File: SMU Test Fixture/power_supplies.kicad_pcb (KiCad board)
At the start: 2 copper layers, 84.9 x 130.1 mm, 47 parts, among them J13 Hot_Spade, J14 Power Outputs, J15 Neutral_Spade, Q1 IRFL014, Q2 IRFL014, T1 VPP28-1060, U10 LT3045, U11 LT1086-12, U12 LT3094, U9 LT1086-5.0

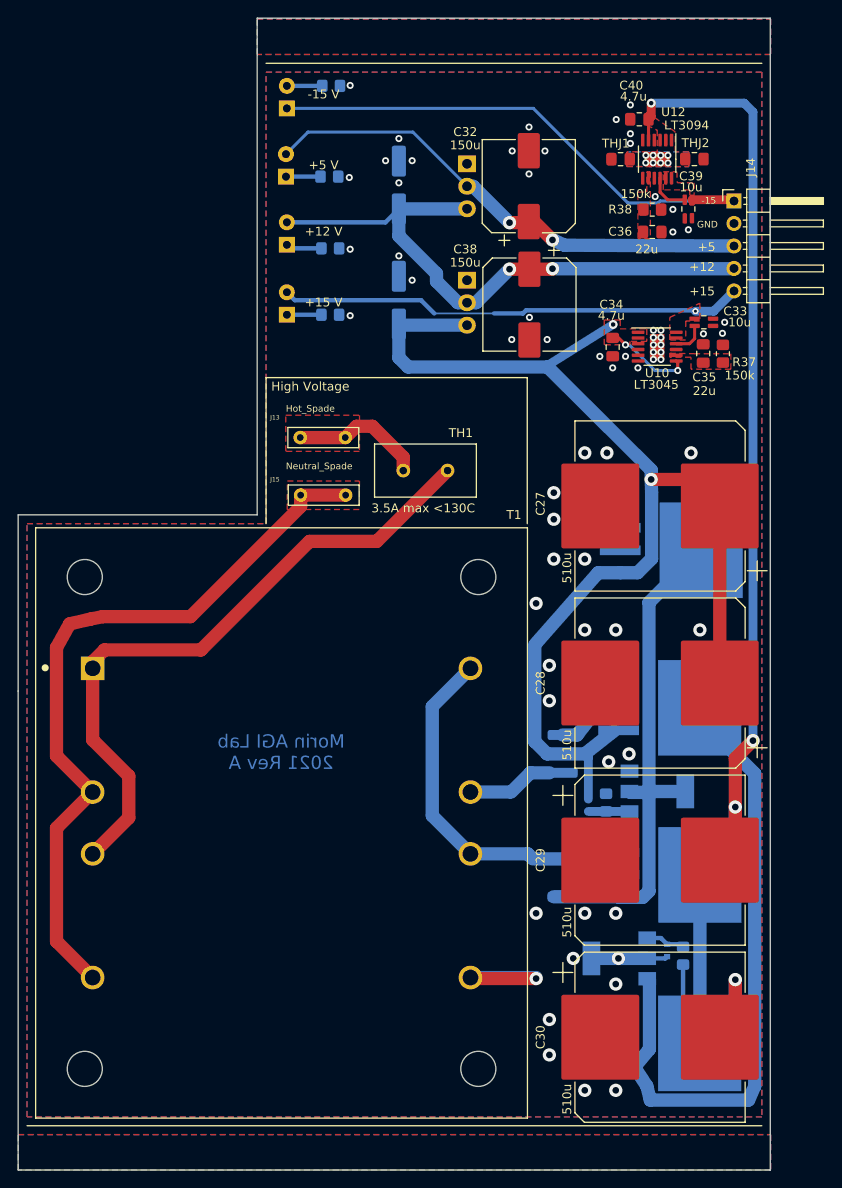
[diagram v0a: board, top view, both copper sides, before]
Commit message: Improved crowbar performance. Posted for reddit design review.
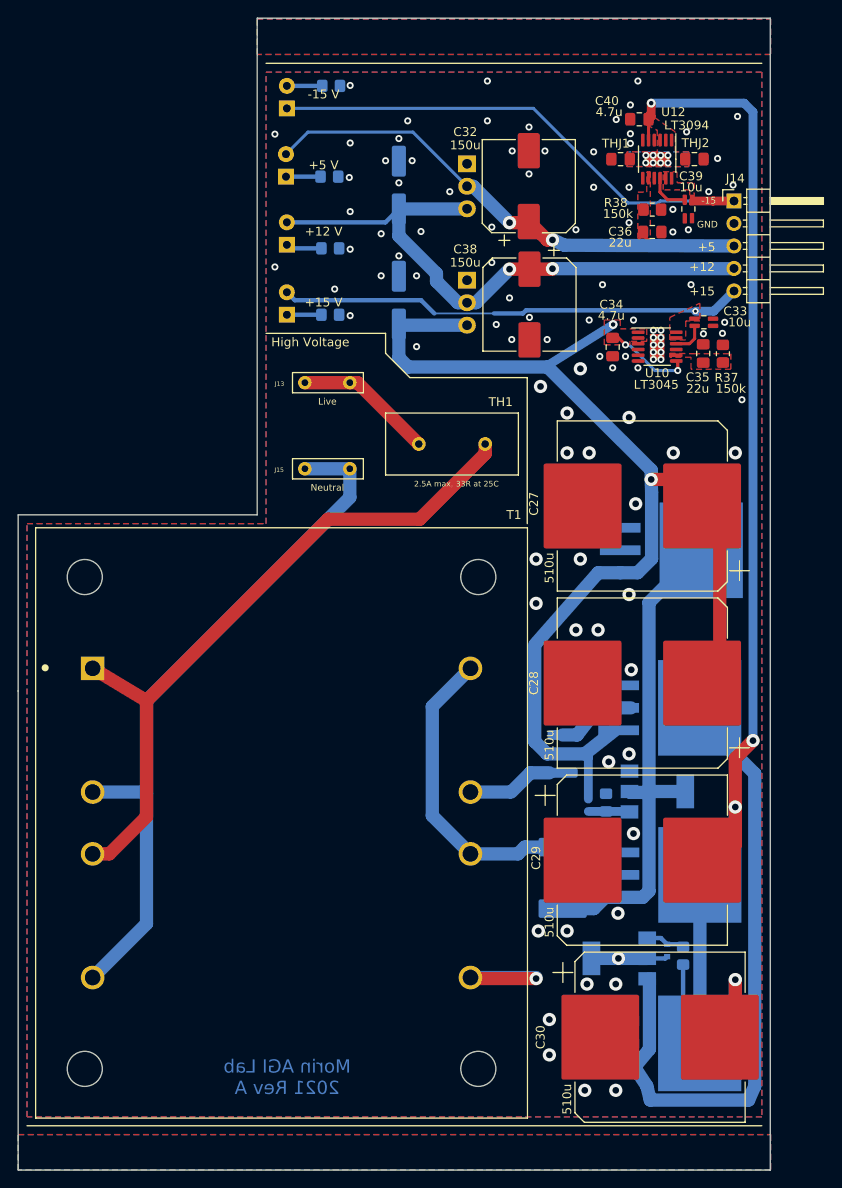
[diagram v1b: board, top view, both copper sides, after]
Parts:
- D39, D46: value 20V -> 16V
- F1: footprint Fuse:Fuse_1812_4532Metric -> Fuse:Fuse_2920_7451Metric_Pad2.10x5.45mm_HandSolder
- F2: value 1 A -> 500mA
- J13: value Hot_Spade -> Live
- J15: value Neutral_Spade -> Neutral
- R39, R40: value 1K -> 180R
- TH1: value 3.5A max <130C -> 2.5A max, 33R at 25C; footprint MAGI_Footprints:NTC d=11.5 p=5mm w=6mm -> MAGI_Footprints:NTC d=15 p=7p5mm w=7mm
- moved J13 6.22 mm to (138.9, 70.2)
- moved TH1 4.24 mm to (153.0, 77.0)
- moved J15 3.01 mm to (138.9, 79.9)
- moved C27 2.00 mm to (174.5, 84.0)
- moved C28 2.00 mm to (174.5, 104.0)
- moved C29 2.00 mm to (174.5, 124.0)
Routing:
- net Net-(T1-Pad1): track 74.1 -> 78.9 mm
- net Net-(J15-Pad1): track 83.1 -> 80.7 mm
- net Net-(J13-Pad1): track 15.1 -> 15.7 mm
- net Net-(F1-Pad2): track 35.8 -> 35.3 mm
- net GND: vias 68 -> 104
- removed copper zone on F.Cu, net Net-(J13-Pad1)
- removed copper zone on F.Cu, net Net-(J15-Pad1)
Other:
- net class HV: clearance 2 -> 4; trace_width 1.5 -> 1; via_dia 1.5 -> 1

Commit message: Route LTC2966 addition and remove pin 2 connections.
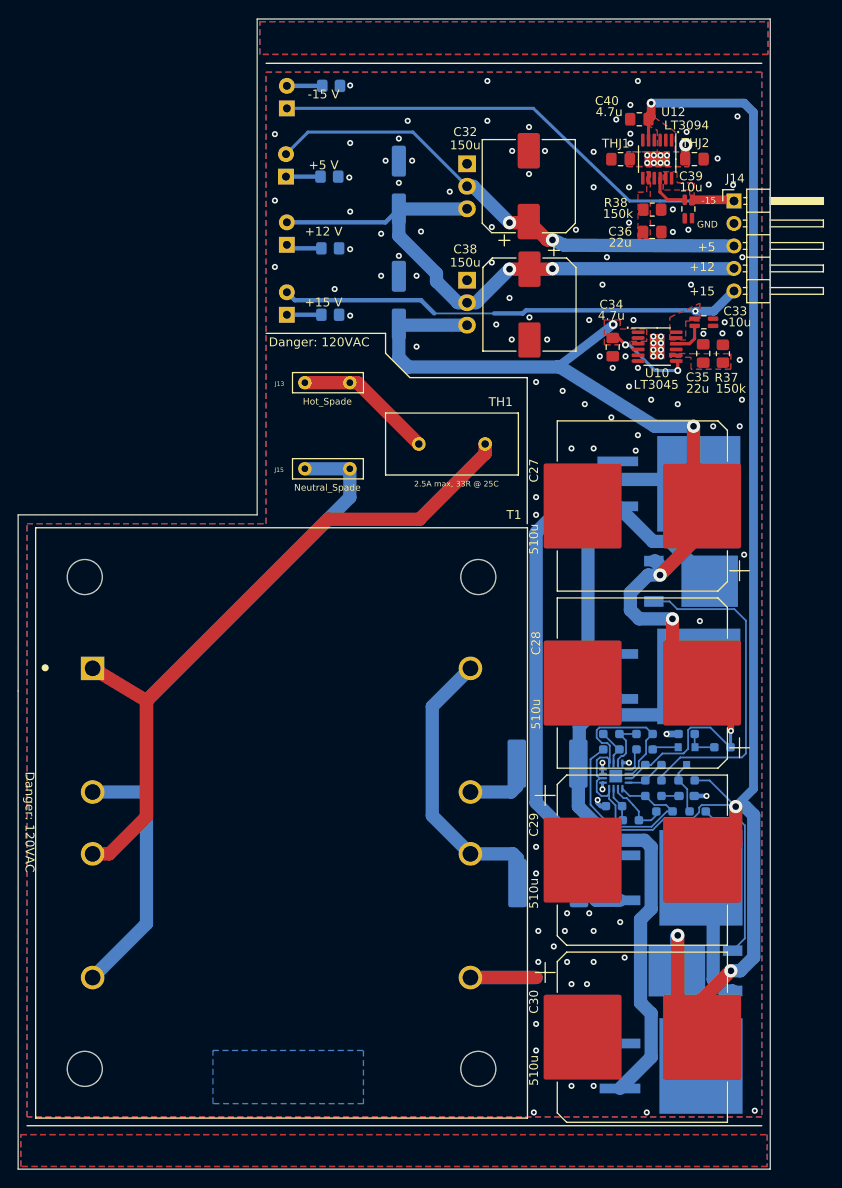
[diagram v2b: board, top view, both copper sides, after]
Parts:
- removed D39, D46: 16V, Diode_SMD:D_SOD-523
- added C41: 1u, Capacitor_SMD:C_0603_1608Metric_Pad1.08x0.95mm_HandSolder, B.Cu at (179.5, 116.8)
- added Q3: MMBT3906, Package_TO_SOT_SMD:SOT-23, B.Cu at (179.5, 112.2)
- added R41: 10K, Resistor_SMD:R_0603_1608Metric_Pad0.98x0.95mm_HandSolder, B.Cu at (183.6, 111.2)
- added R42: 1.5K, Resistor_SMD:R_0603_1608Metric_Pad0.98x0.95mm_HandSolder, B.Cu at (173.2, 119.5)
- added R43: 100R, Resistor_SMD:R_0603_1608Metric_Pad0.98x0.95mm_HandSolder, B.Cu at (174.8, 111.5)
- added R44: 10K, Resistor_SMD:R_0603_1608Metric_Pad0.98x0.95mm_HandSolder, B.Cu at (179.5, 109.8)
- added R45: 21.5K, Resistor_SMD:R_0603_1608Metric_Pad0.98x0.95mm_HandSolder, B.Cu at (174.8, 109.8)
- added R46: 20K, Resistor_SMD:R_0603_1608Metric_Pad0.98x0.95mm_HandSolder, B.Cu at (171.3, 117.9)
- added R47: 2.43K, Resistor_SMD:R_0603_1608Metric_Pad0.98x0.95mm_HandSolder, B.Cu at (171.0, 109.8)
- added R48: 215K, Resistor_SMD:R_0603_1608Metric_Pad0.98x0.95mm_HandSolder, B.Cu at (171.0, 111.5)
- added R49: 600R, Resistor_SMD:R_0603_1608Metric_Pad0.98x0.95mm_HandSolder, B.Cu at (175.8, 116.8)
- added R50: 250K, Resistor_SMD:R_0603_1608Metric_Pad0.98x0.95mm_HandSolder, B.Cu at (175.8, 113.2)
- added R51: 100R, Resistor_SMD:R_0603_1608Metric_Pad0.98x0.95mm_HandSolder, B.Cu at (180.8, 118.5)
- added R52: 10k, Resistor_SMD:R_0603_1608Metric_Pad0.98x0.95mm_HandSolder, B.Cu at (179.5, 115.0)
- added U13: LTC2966CSWPBF, Package_DFN_QFN:QFN-16-1EP_3x3mm_P0.5mm_EP1.45x1.45mm, B.Cu at (171.5, 114.5)
- D37, D38, D40, D41: footprint Package_TO_SOT_SMD:TO-263-3_TabPin2 -> Package_TO_SOT_SMD:TO-263-2
- F1: value 1 A -> 3.7 A
- F2: value 500mA -> 3.7 A; footprint Fuse:Fuse_1812_4532Metric -> Fuse:Fuse_2920_7451Metric_Pad2.10x5.45mm_HandSolder
- J13: value Live -> Hot_Spade
- J15: value Neutral -> Neutral_Spade
- Q1: value IRFL014 -> IRLR6225TRPBF; footprint Package_TO_SOT_SMD:SOT-223 -> Package_TO_SOT_SMD:TO-252-2
- Q2: value IRFL014 -> NTD3055-150T4G; footprint Package_TO_SOT_SMD:SOT-223 -> Package_TO_SOT_SMD:TO-252-2
- R39: value 180R -> 100R; footprint Resistor_SMD:R_0805_2012Metric_Pad1.20x1.40mm_HandSolder -> Resistor_SMD:R_0603_1608Metric_Pad0.98x0.95mm_HandSolder
- R40: value 180R -> 2.55K; footprint Resistor_SMD:R_0805_2012Metric_Pad1.20x1.40mm_HandSolder -> Resistor_SMD:R_0603_1608Metric_Pad0.98x0.95mm_HandSolder
- TH1: value 2.5A max, 33R at 25C -> 2.5A max, 33R @ 25C
- moved Q1 43.4 mm to (180.0, 92.5), turned to 0 degrees
- moved Q2 20.7 mm to (180.5, 136.5), turned to 180 degrees
- moved R39 20.1 mm to (175.8, 115.0), turned to 180 degrees
- moved D37 7.51 mm to (177.5, 81.5)
- moved R40 6.68 mm to (177.0, 118.5), turned to 180 degrees
- moved D38 3.55 mm to (177.5, 103.2)
- moved D41 2.55 mm to (177.8, 147.2)
- moved F2 2.02 mm to (163.8, 113.1), turned to 180 degrees
- moved C30 2.00 mm to (174.5, 144.0)
- moved F1 1.73 mm to (163.9, 126.6), turned to 180 degrees
- moved D40 0.36 mm to (177.8, 126.0)
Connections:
- net Net-(D46-Pad2) renamed /pos_disable
- D37 pad 1: /unreg_pos_18VDC -> Net-(D37-Pad1)
- D37 pad 2: /unfilt_pos -> Net-(D37-Pad2)
- D38 pad 1: /unreg_pos_18VDC -> Net-(D37-Pad1)
- D38 pad 2: /unfilt_neg -> Net-(D38-Pad2)
- D40 pad 1: /unfilt_pos -> Net-(D37-Pad2)
- D40 pad 2: /unreg_neg_18VDC -> Net-(D40-Pad2)
- D41 pad 1: /unfilt_neg -> Net-(D38-Pad2)
- D41 pad 2: /unreg_neg_18VDC -> Net-(D40-Pad2)
- F1 pad 1: /unfilt_pos -> Net-(D37-Pad2)
- F2 pad 1: /unfilt_neg -> Net-(D38-Pad2)
- Q1 pad 2: GND -> Net-(D37-Pad1)
- Q1 pad 3: /unfilt_neg -> /unreg_pos_18VDC
- Q2 pad 1: Net-(D39-Pad2) -> /neg_disable
- Q2 pad 2: /unfilt_pos -> /unreg_neg_18VDC
- Q2 pad 3: GND -> Net-(D40-Pad2)
- R39 pad 2: /unreg_neg_18VDC -> Net-(R39-Pad2)
- R40 pad 1: Net-(D39-Pad2) -> /ovp_ref
- R40 pad 2: GND -> Net-(R40-Pad2)
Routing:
- net /unfilt_neg: track 88.5 -> 0.00 mm
- net Net-(D37-Pad2): track 0.00 -> 68.1 mm
- net Net-(D38-Pad2): track 0.00 -> 65.0 mm
- net /unfilt_pos: track 57.9 -> 0.00 mm
- net /ovp_ref: track 0.00 -> 44.2 mm
- net Net-(D37-Pad1): track 0.00 -> 38.4 mm
- net /pos_disable: track 4.46 -> 37.4 mm
- net /unreg_neg_18VDC: track 154.3 -> 183.6 mm, vias 12 -> 13
- net Net-(D40-Pad2): track 0.00 -> 24.8 mm
- net /unreg_pos_18VDC: track 151.2 -> 130.3 mm, vias 4 -> 7
- net /neg_disable: track 0.00 -> 19.8 mm
- net Net-(R40-Pad2): track 0.00 -> 7.35 mm
- net Net-(Q3-Pad3): track 0.00 -> 6.15 mm
- net Net-(R45-Pad2): track 0.00 -> 6.05 mm
- net Net-(D39-Pad2): track 4.67 -> 0.00 mm
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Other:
- board size 84.9 x 130.1 mm -> 84.9 x 129.9 mm
- board text added: "."
- board text added: "18VAC"
- board text added: "CT"
- board text added: "Danger: 120VAC"
- board text removed: "High Voltage"

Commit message: Silkscreen fixes
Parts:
- F1, F2: value 3.7 A -> 3.7A
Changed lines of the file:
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@@
   (page A4)
   (layers
-    (0 F.Cu power)
+    (0 F.Cu power hide)
     (31 B.Cu power)
     (36 B.SilkS user)
-    (37 F.SilkS user)
+    (37 F.SilkS user hide)
     (38 B.Mask user)
-    (39 F.Mask user)
+    (39 F.Mask user hide)
     (41 Cmts.User user)
     (44 Edge.Cuts user)
@@
     (tags "resistor handsolder")
     (attr smd)
-    (fp_text reference R51 (at 2.7 -0.4) (layer B.SilkS)
-      (effects (font (size 0.55 0.55) (thickness 0.127)) (justify mirror))
-    )
-    (fp_text value 100R (at 3 0.45) (layer B.SilkS)
+    (fp_text reference R51 (at 2.45 -0.65) (layer B.SilkS)
+      (effects (font (size 0.55 0.55) (thickness 0.127)) (justify mirror))
+    )
+    (fp_text value 100R (at 2.75 0.2) (layer B.SilkS)
       (effects (font (size 0.55 0.55) (thickness 0.127)) (justify mirror))
     )
@@
     (tags "D2PAK DDPAK TO-263 D2PAK-3 TO-263-3 SOT-404")
     (attr smd)
-    (fp_text reference D37 (at 0 6.65) (layer B.SilkS)
+    (fp_text reference D37 (at 6.5 -6.25 180) (layer B.SilkS)
       (effects (font (size 1 1) (thickness 0.15)) (justify mirror))
     )
@@
       (effects (font (size 1 1) (thickness 0.15)) (justify mirror))
     )
-    (fp_text value "3.7 A" (at 5.875 -0.9 90) (layer B.SilkS)
+    (fp_text value 3.7A (at 5.875 -0.9 90) (layer B.SilkS)
       (effects (font (size 1 1) (thickness 0.15)) (justify mirror))
     )
@@
     (tags "DPAK TO-252 DPAK-3 TO-252-3 SOT-428")
     (attr smd)
-    (fp_text reference Q2 (at 0 4.5) (layer B.SilkS)
+    (fp_text reference Q2 (at -6.5 0.25 180) (layer B.SilkS)
       (effects (font (size 1 1) (thickness 0.15)) (justify mirror))
     )
@@
     (tags "DPAK TO-252 DPAK-3 TO-252-3 SOT-428")
     (attr smd)
-    (fp_text reference Q1 (at 0 4.5) (layer B.SilkS)
+    (fp_text reference Q1 (at 6.5 0 180) (layer B.SilkS)
       (effects (font (size 1 1) (thickness 0.15)) (justify mirror))
     )
@@
     (tags "D2PAK DDPAK TO-263 D2PAK-3 TO-263-3 SOT-404")
     (attr smd)
-    (fp_text reference D41 (at 0 6.65) (layer B.SilkS)
+    (fp_text reference D41 (at 6.25 -6.25 180) (layer B.SilkS)
       (effects (font (size 1 1) (thickness 0.15)) (justify mirror))
     )
@@
     (tags "D2PAK DDPAK TO-263 D2PAK-3 TO-263-3 SOT-404")
     (attr smd)
-    (fp_text reference D40 (at 0 6.65) (layer B.SilkS)
+    (fp_text reference D40 (at 6.25 -6.25 180) (layer B.SilkS)
       (effects (font (size 1 1) (thickness 0.15)) (justify mirror))
     )
@@
     (tags "D2PAK DDPAK TO-263 D2PAK-3 TO-263-3 SOT-404")
     (attr smd)
-    (fp_text reference D38 (at 7.1 6.35) (layer B.SilkS)
+    (fp_text reference D38 (at 6 -6.25 180) (layer B.SilkS)
       (effects (font (size 1 1) (thickness 0.15)) (justify mirror))
     )
@@
       (effects (font (size 1 1) (thickness 0.15)) (justify mirror))
     )
-    (fp_text value "3.7 A" (at 5.8 -1.4 270) (layer B.SilkS)
+    (fp_text value 3.7A (at 5.8 -1.4 270) (layer B.SilkS)
       (effects (font (size 1 1) (thickness 0.15) italic) (justify mirror))
     )
@@
     (descr "LED, diameter 3.0mm z-position of LED center 2.0mm, 2 pins, diameter 3.0mm z-position of LED center 2.0mm, 2 pins, diameter 3.0mm z-position of LED center 2.0mm, 2 pins")
     (tags "LED diameter 3.0mm z-position of LED center 2.0mm 2 pins diameter 3.0mm z-position of LED center 2.0mm 2 pins diameter 3.0mm z-position of LED center 2.0mm 2 pins")
-    (fp_text reference D45 (at -2.05 0) (layer B.SilkS)
+    (fp_text reference D45 (at -1.75 0) (layer B.SilkS)
       (effects (font (size 1 1) (thickness 0.15)) (justify mirror))
     )
@@
     (descr "LED, diameter 3.0mm z-position of LED center 2.0mm, 2 pins, diameter 3.0mm z-position of LED center 2.0mm, 2 pins, diameter 3.0mm z-position of LED center 2.0mm, 2 pins")
     (tags "LED diameter 3.0mm z-position of LED center 2.0mm 2 pins diameter 3.0mm z-position of LED center 2.0mm 2 pins diameter 3.0mm z-position of LED center 2.0mm 2 pins")
-    (fp_text reference D42 (at 4.4 0) (layer B.SilkS)
+    (fp_text reference D42 (at 4.15 0) (layer B.SilkS)
       (effects (font (size 1 1) (thickness 0.15)) (justify mirror))
     )
@@
       (effects (font (size 1 1) (thickness 0.15)) (justify mirror))
     )
-    (fp_text value 750R (at 4.65 -0.05) (layer B.SilkS)
-      (effects (font (size 1 1) (thickness 0.15)) (justify mirror))
-    )
+    (fp_text value 750R (at 0.15 -1.55) (layer B.SilkS)
+      (effects (font (size 1 1) (thickness 0.15)) (justify mirror))
+    )
